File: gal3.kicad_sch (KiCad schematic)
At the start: 9 parts, among them IC13 SN74ALS374N, IC22 SN74LS74N, IC8 SN74ALS374N, IC9 D65200GD076

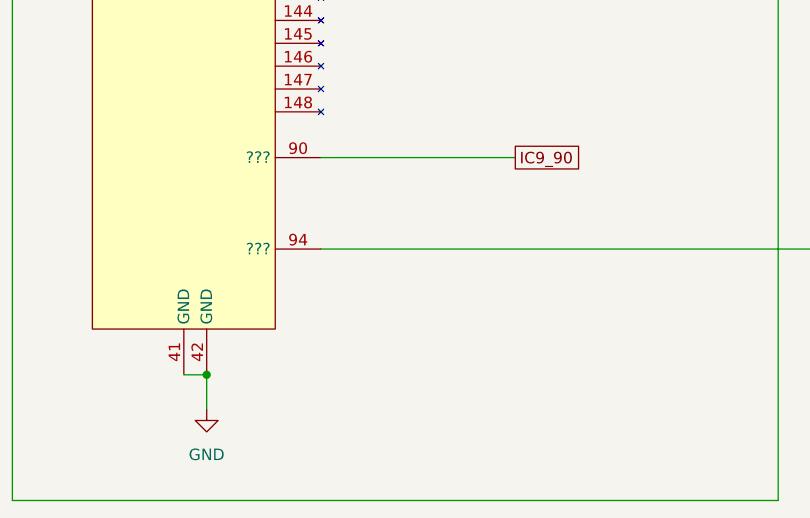
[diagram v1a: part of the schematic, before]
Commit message: pcb, schematic: wire IC9 pin 96
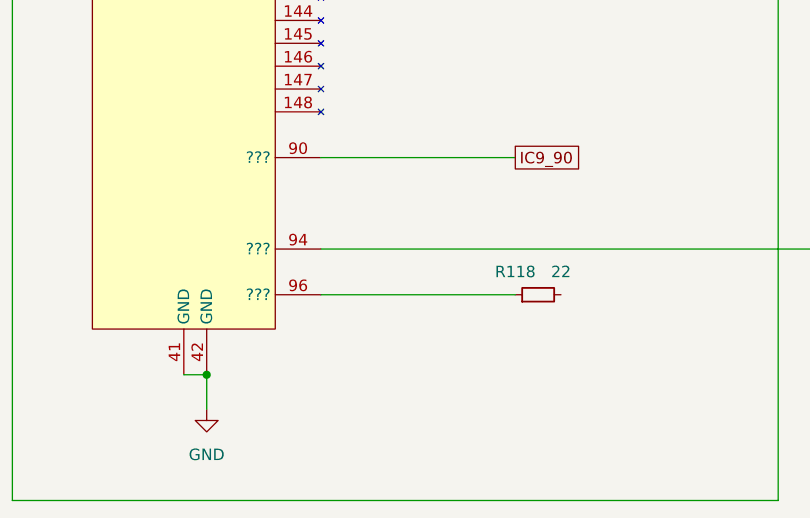
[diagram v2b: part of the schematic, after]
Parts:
- added R118: 22, Resistor_SMD:R_1206_3216Metric, symbol Device:R_Small
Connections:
- new net: IC9.96 (???), R118.1
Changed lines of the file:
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@@
+    (stroke (width 0) (type default))
+  )
+  (wire (pts (xy 67.31 358.14) (xy 88.9 358.14))
     (stroke (width 0) (type default))
   )
@@
     (property "Intersheetrefs" "${INTERSHEET_REFS}" (at 176.6123 209.55 0)
       (effects (font (size 1.27 1.27)) (justify left) hide)
+    )
+  )
+  (symbol (lib_id "Device:R_Small") (at 91.44 358.14 90) (unit 1)
+    (in_bom yes) (on_board yes) (dnp no)
+    (property "Reference" "R118" (at 88.9 355.6 90)
+      (effects (font (size 1.27 1.27)))
+    )
+    (property "Value" "22" (at 93.98 355.6 90)
+      (effects (font (size 1.27 1.27)))
+    )
+    (property "Footprint" "Resistor_SMD:R_1206_3216Metric" (at 91.44 358.14 0)
+      (effects (font (size 1.27 1.27)) hide)
+    )
+    (property "Datasheet" "~" (at 91.44 358.14 0)
+      (effects (font (size 1.27 1.27)) hide)
+    )
+    (pin "2")
+    (pin "1")
+    (instances
+      (project "88va2-circuit"
+        (path "/8cd193ae-a369-4130-9ba4-f2075fa60e2b/69b5e096-b79d-4084-a9d7-aa17e9aa2515"
+          (reference "R118") (unit 1)
+        )
+      )
     )
   )
@@
     (pin "90")
     (pin "94")
+    (pin "96")
     (instances
       (project "88va2-circuit"

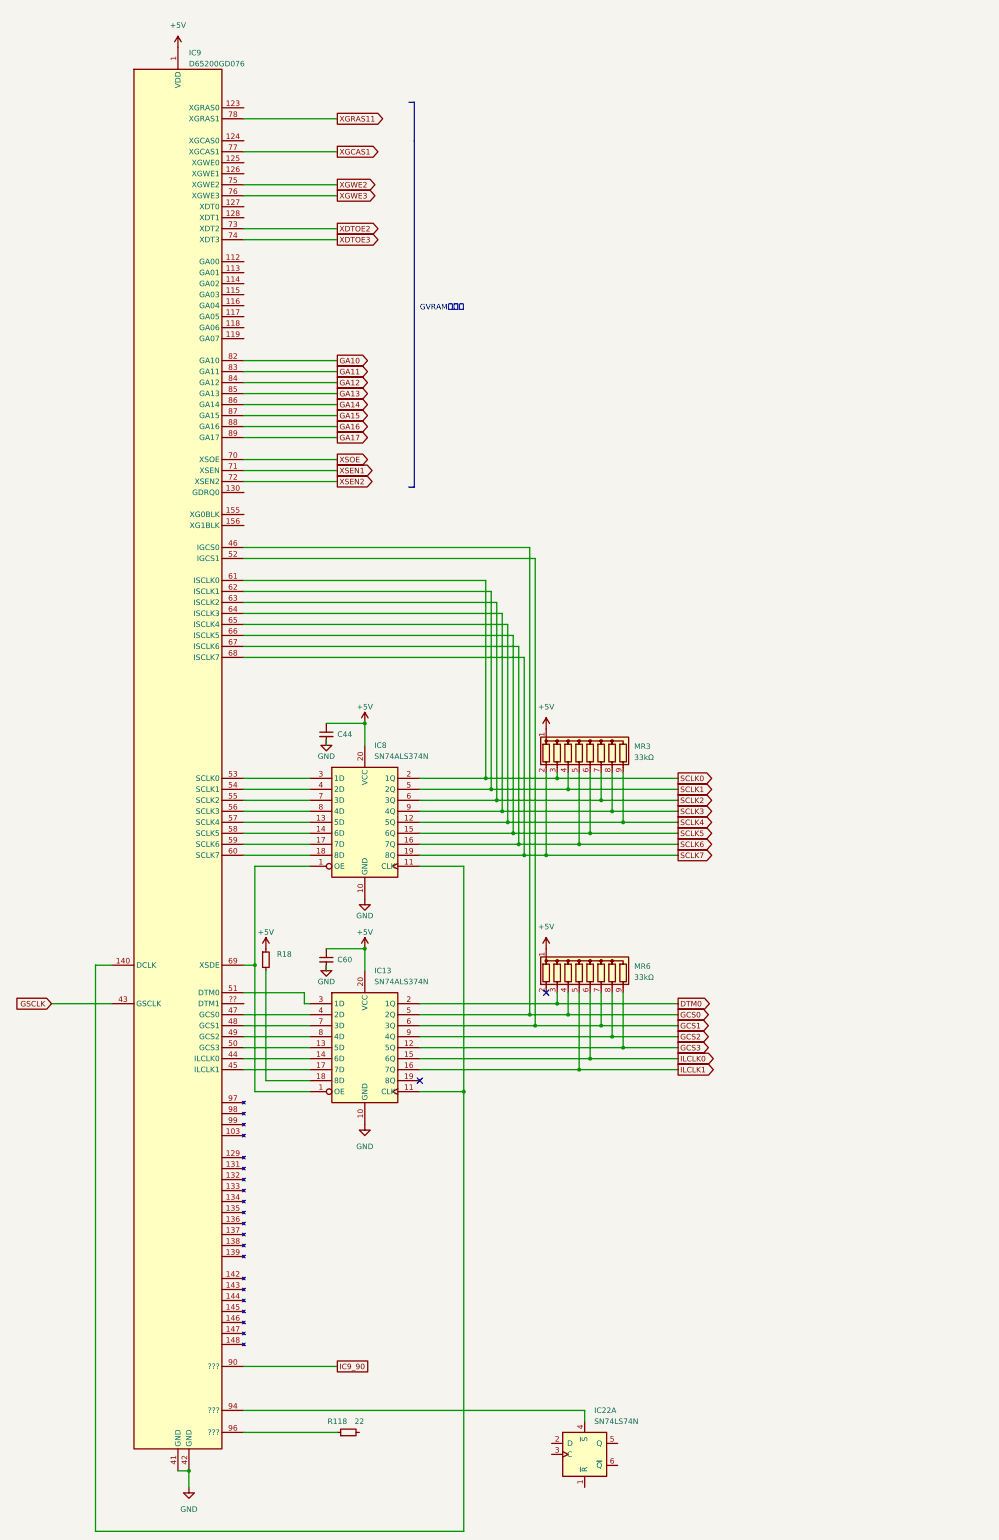
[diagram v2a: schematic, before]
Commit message: schematic: add lines from IC9 to GVRAM1-4
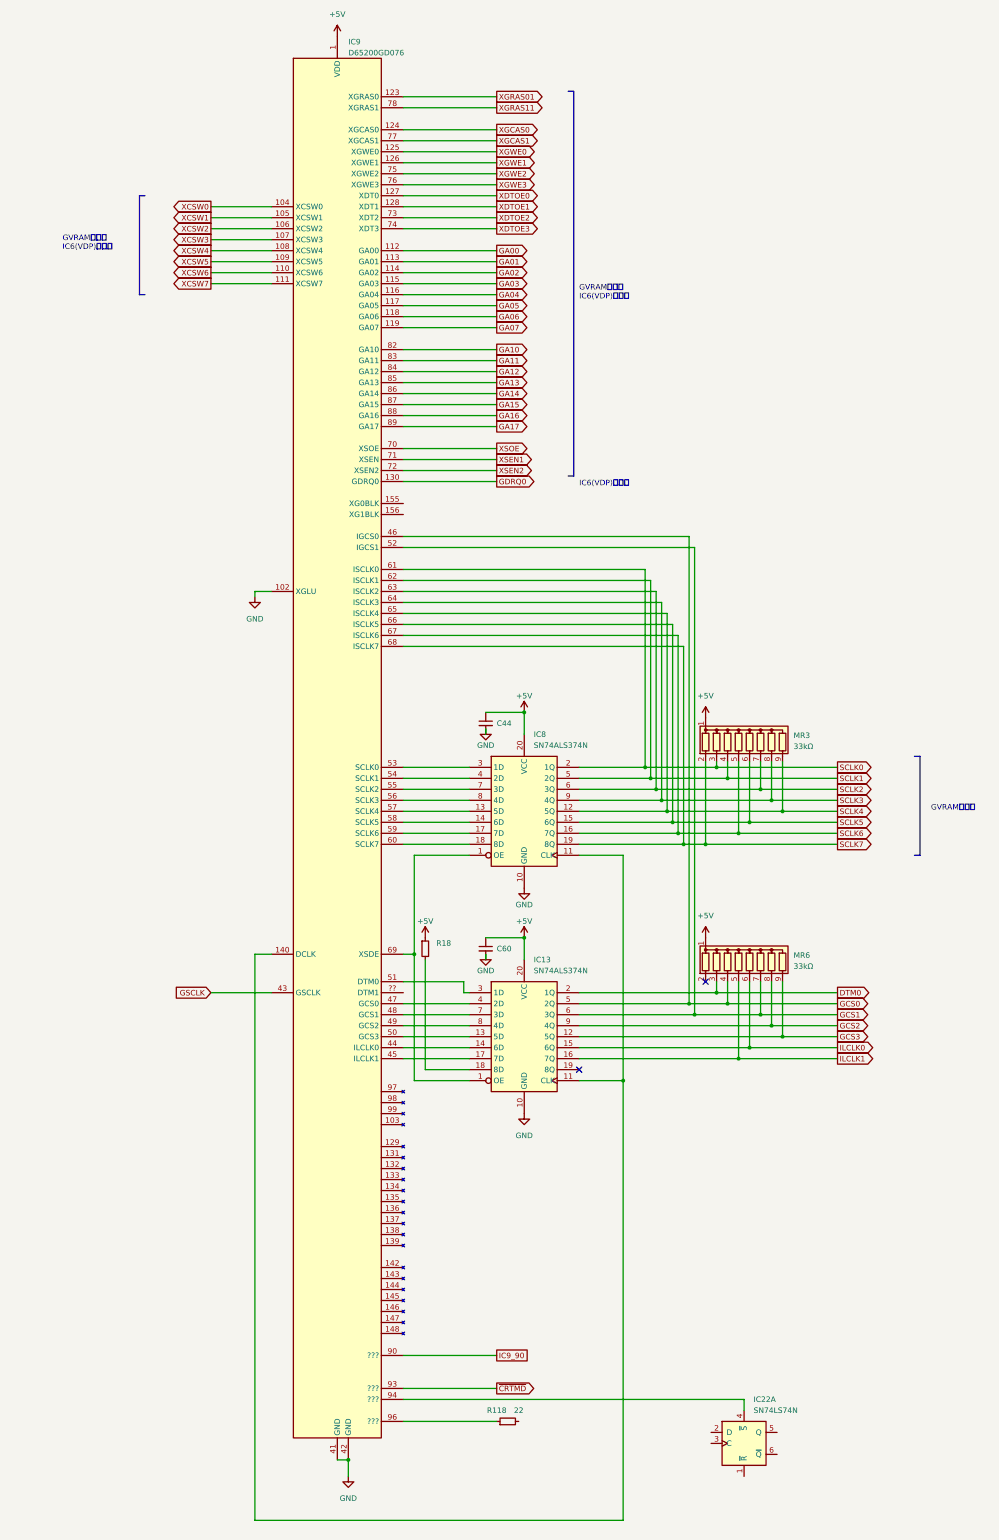
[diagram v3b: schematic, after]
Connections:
- net GND: now also IC9.102 (XGLU)
- net GA00: now reaches IC9.112 (GA00)
- net GA01: now reaches IC9.113 (GA01)
- net GA02: now reaches IC9.114 (GA02)
- net GA03: now reaches IC9.115 (GA03)
- net GA04: now reaches IC9.116 (GA04)
- net GA05: now reaches IC9.117 (GA05)
- net GA06: now reaches IC9.118 (GA06)
- net GA07: now reaches IC9.119 (GA07)
- net XGRAS01: now reaches IC9.123 (XGRAS0)
- net XGCAS0: now reaches IC9.124 (XGCAS0)
- net XGWE0: now reaches IC9.125 (XGWE0)
- net XGWE1: now reaches IC9.126 (XGWE1)
- net XDTOE0: now reaches IC9.127 (XDT0)
- net XDTOE1: now reaches IC9.128 (XDT1)
- net GDRQ0: now reaches IC9.130 (GDRQ0)
- new net XCSW0: IC9.104 (XCSW0)
- new net XCSW1: IC9.105 (XCSW1)
- new net XCSW2: IC9.106 (XCSW2)
- new net XCSW3: IC9.107 (XCSW3)
- new net XCSW4: IC9.108 (XCSW4)
- new net XCSW5: IC9.109 (XCSW5)
- new net XCSW6: IC9.110 (XCSW6)
- new net XCSW7: IC9.111 (XCSW7)
- new net ~{CRTMD}: IC9.93 (???)
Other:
- note added: "GVRAMへ接続 IC6(VDP)と共有"
- note added: "IC6(VDP)へ接続"
- moved on the sheet: C44, C60, IC13, IC22A, IC8, MR3, MR6, R118, R18

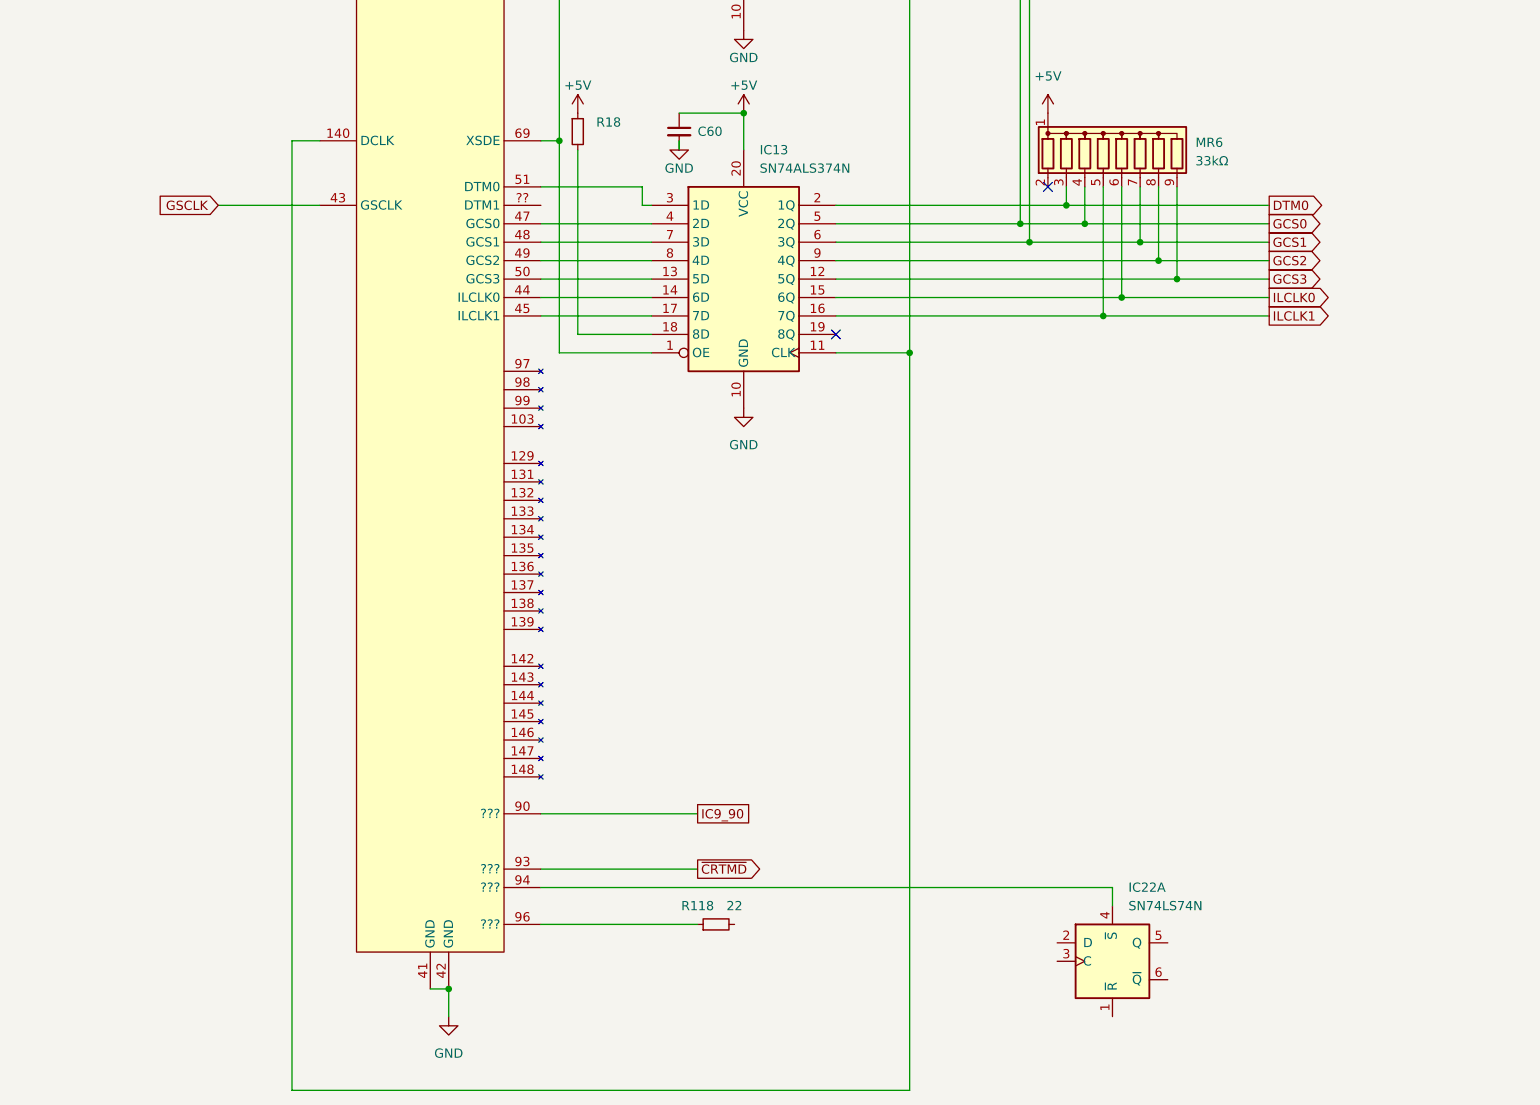
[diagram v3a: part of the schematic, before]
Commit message: add display clock generator
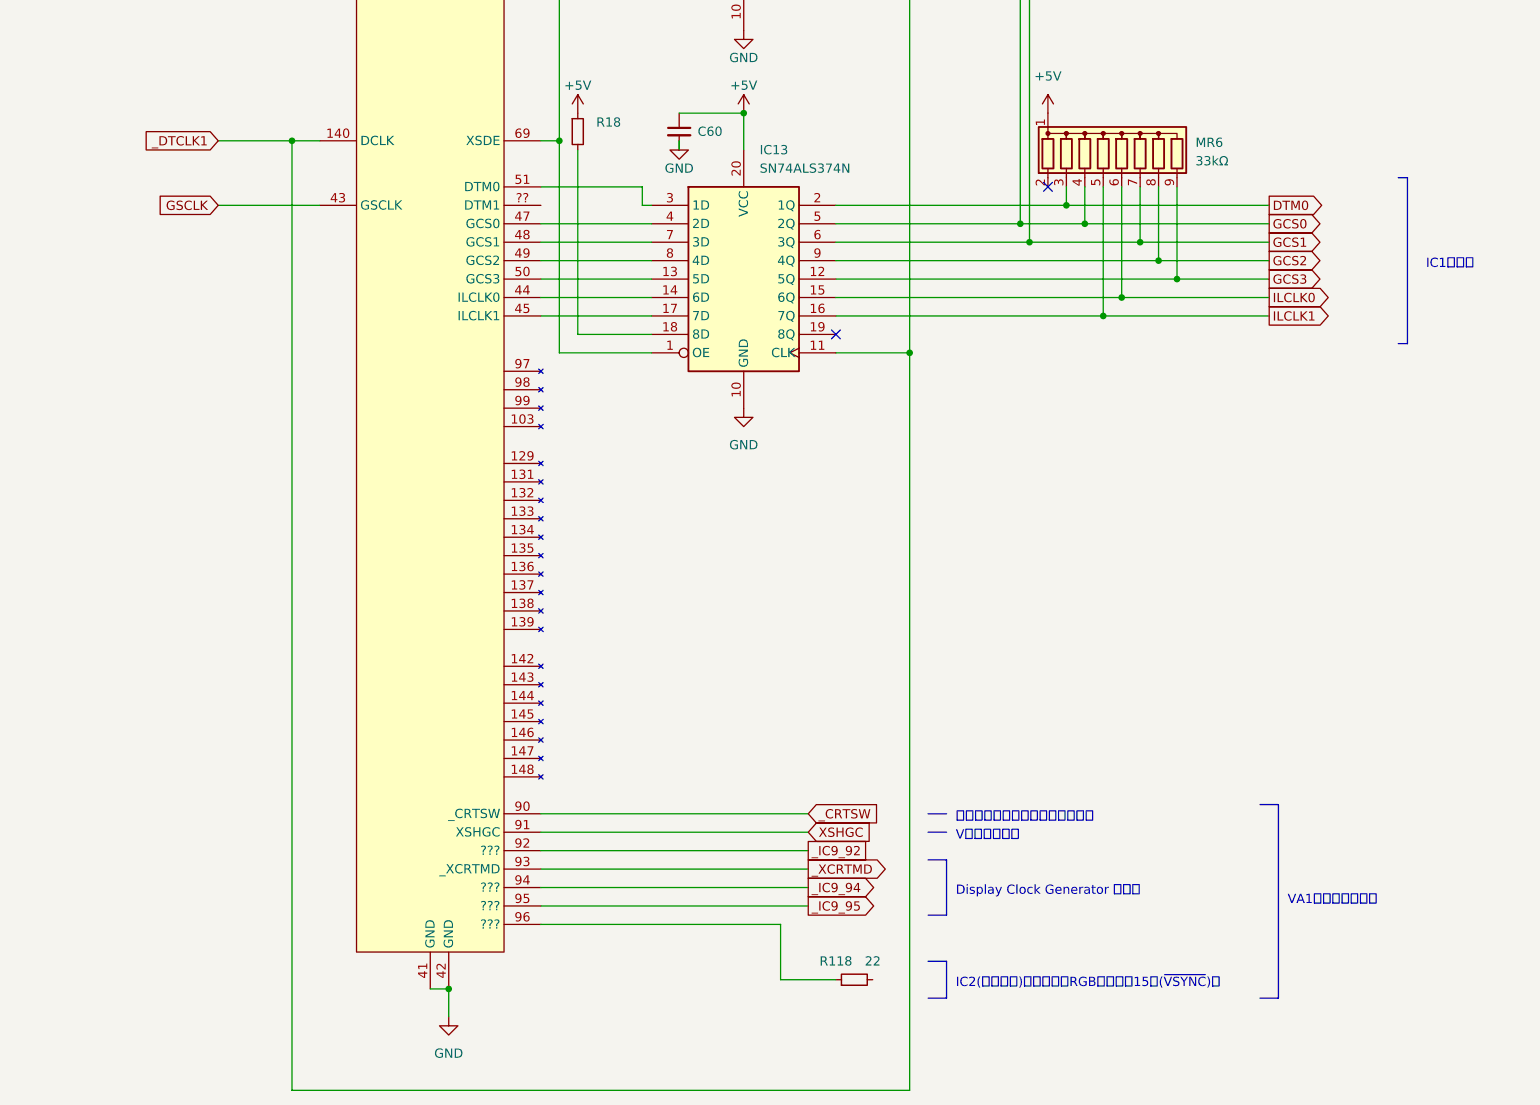
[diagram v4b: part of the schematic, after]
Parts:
- removed IC22: SN74LS74N, Package_DIP:DIP-14_W7.62mm, symbol 74xx:74LS74
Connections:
- net _DTCLK1: now reaches IC13.11 (CLK), IC8.11 (CLK), IC9.140 (DCLK)
- net _IC9_94: now reaches IC9.94 (???)
- net IC9_90 renamed _CRTSW
- net ~{CRTMD} renamed _XCRTMD
- new net XSHGC: IC9.91 (XSHGC)
- new net _IC9_92: IC9.92 (???)
- new net _IC9_95: IC9.95 (???)
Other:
- note added: "Display Clock Generator へ接続"
- note added: "IC1へ接続"
- note added: "IC2(バッファ)を経由してRGBコネクタ15番(~{VSYNC})へ"
- note added: "VA1回路図には無い"
- note added: "Vスロットから"
- note added: "ディスプレイモード切替スイッチ"
- moved on the sheet: R118

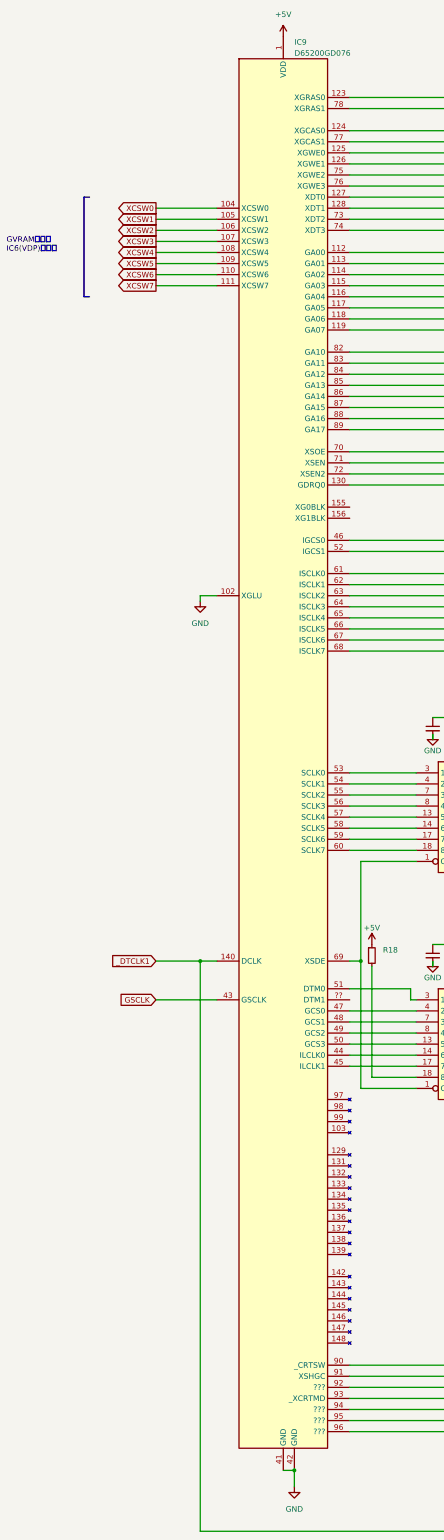
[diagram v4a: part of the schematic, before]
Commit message: pcb: fix some DRC check errors
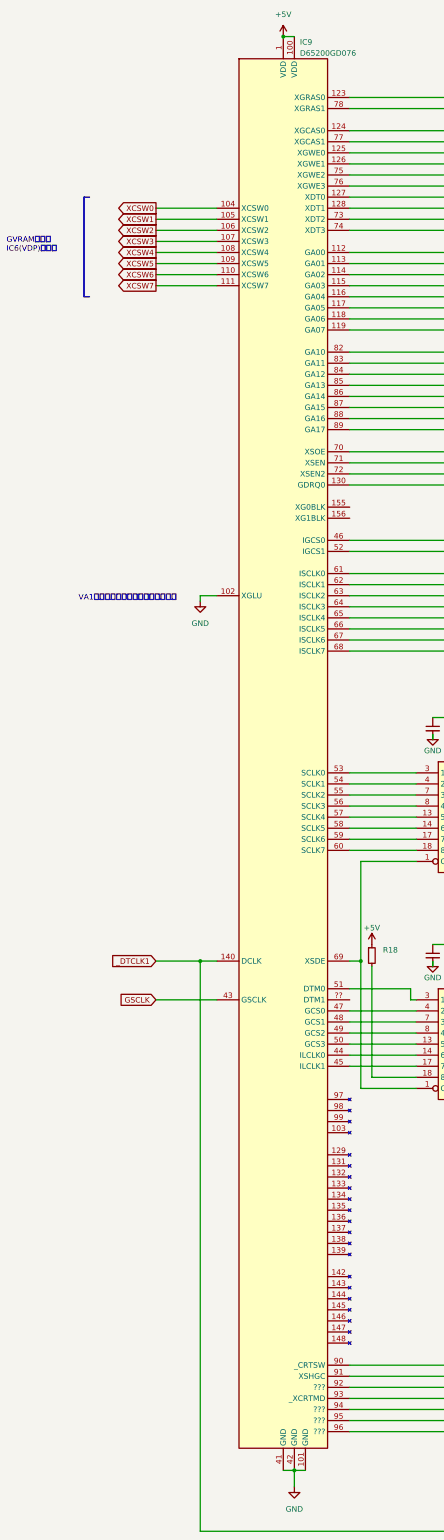
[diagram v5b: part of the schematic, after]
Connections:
- net +5V: now also IC9.100 (VDD)
- net GND: now also IC9.101 (GND)
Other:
- note added: "VA1回路図ではプルアップされている"
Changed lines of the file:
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@@
   (junction (at 186.69 209.55) (diameter 0) (color 0 0 0 0)
+  )
+  (junction (at 88.9 35.56) (diameter 0) (color 0 0 0 0)
   )
   (junction (at 132.08 191.77) (diameter 0) (color 0 0 0 0)
@@
     (stroke (width 0) (type default))
   )
+  (wire (pts (xy 91.44 364.49) (xy 93.98 364.49))
+    (stroke (width 0) (type default))
+  )
   (wire (pts (xy 176.53 203.2) (xy 176.53 204.47))
     (stroke (width 0) (type default))
@@
   )
   (wire (pts (xy 144.78 212.09) (xy 163.83 212.09))
+    (stroke (width 0) (type default))
+  )
+  (wire (pts (xy 88.9 35.56) (xy 91.44 35.56))
     (stroke (width 0) (type default))
   )
@@
   )
   (text "Display Clock Generator へ接続" (at 161.29 351.79 0)
+    (effects (font (size 1.27 1.27)) (justify left bottom))
+  )
+  (text "VA1回路図ではプルアップされている" (at 41.91 165.1 0)
     (effects (font (size 1.27 1.27)) (justify left bottom))
   )
@@
   (symbol (lib_id "88va_Library:GAL") (at 88.9 186.69 0) (unit 1)
     (in_bom yes) (on_board yes) (dnp no) (fields_autoplaced)
-    (property "Reference" "IC9" (at 91.44 36.83 0)
+    (property "Reference" "IC9" (at 92.71 36.83 0)
       (effects (font (size 1.27 1.27)) (justify left))
     )
-    (property "Value" "D65200GD076" (at 91.44 39.37 0)
+    (property "Value" "D65200GD076" (at 92.71 39.37 0)
       (effects (font (size 1.27 1.27)) (justify left))
     )
@@
     (pin "92")
     (pin "95")
+    (pin "101")
+    (pin "100")
     (instances
       (project "88va2-circuit"
